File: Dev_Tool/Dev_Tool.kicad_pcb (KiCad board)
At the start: 4 copper layers, 159.8 x 100 mm, 146 parts, among them J1 UE27-BC54-100, J10 Conn_02x02_Odd_Even, J11 Conn_01x01_Pin, J12 Conn_01x01_Pin, J13 Conn_01x01_Pin, J14 Conn_01x01_Pin, J2 GSB12121031EU, J3 Conn_01x04, J4 95501-2881, J5 95501-2881, J6 JTAG, J7 Conn_02x08_Odd_Even, J8 Conn_02x08_Odd_Even, J9 Conn_02x04_Odd_Even, Q1 BSS138, Q2 BSS138, SW1 SW_Push, U1 USB2514B-AEZC, U10 EPM7032SLC44-10, U11 SN74HCT245DWR, U12 SN74LVC1G07DBV, U13 SN74LVC1G07DBV, U14 SN74LVC1G07DBV, U15 SN74LVC1G07DBV, U16 SN74LVC1G07DBV, U17 SN74LVC1G07DBV, U18 SN74LVC1G07DBV, U19 SN74LVC1G07DBV, U2 MIC2026-1YM, U20 SN74LVC1G07DBV, U21 SN74LVC1G07DBV, U22 SN74LVC1G07DBV, U23 LM1117-3.3, U24 APX803-31SAG-7, U25 SN74LVC1G07DBV, U26 USBLC6-2SC6, U27 USBLC6-2SC6, U3 24C02C-I/P, U4 MCP2221A-I/ST, U5 PCA9535PW, U6 FT232RNL, U7 MAX3243ECDB, U8 FT232RNL, U9 MAX3243ECDB, X1 DIN41612_03x32_ABC_COMETbus, Y1 ECS-3963-240-BN

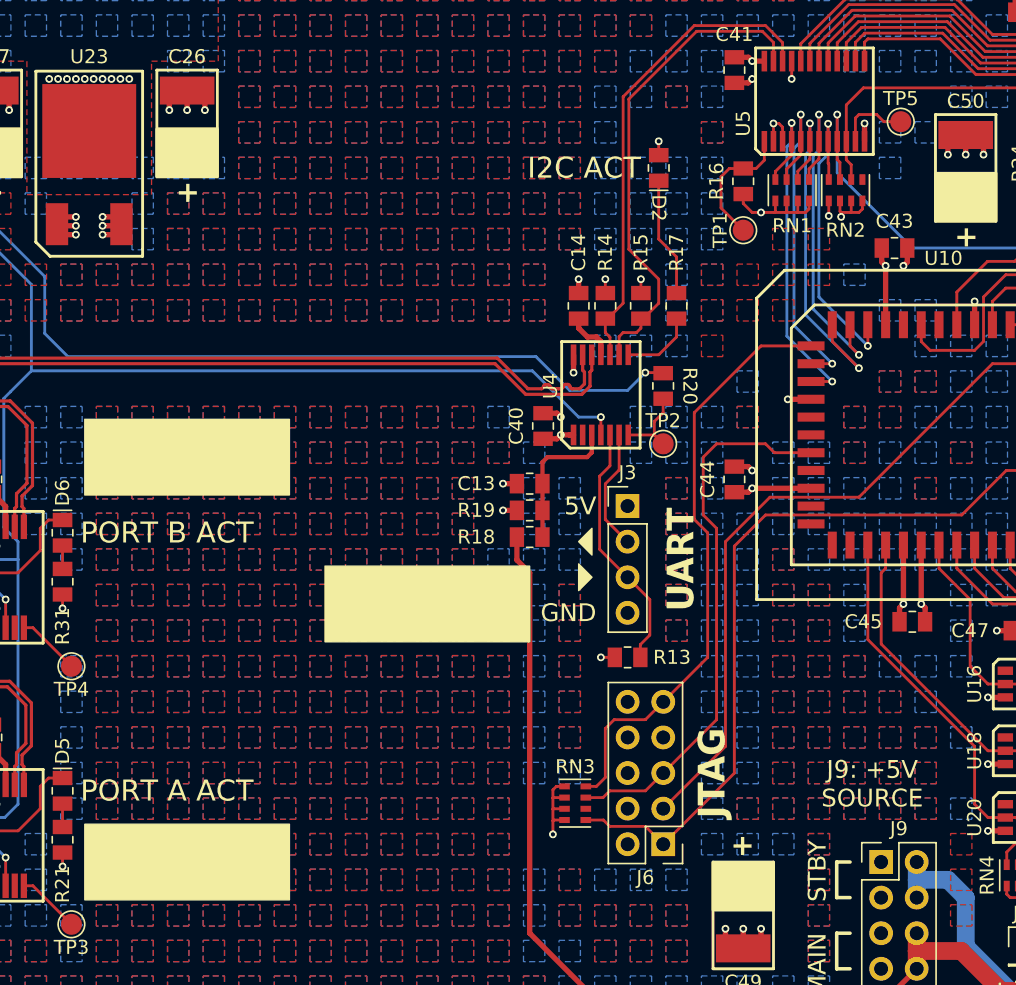
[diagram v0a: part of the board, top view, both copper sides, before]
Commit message: Further changes for rev 2
* Since the IN USE LED was moved to the MCP2221A, this freed up a GPIO on the PCA9535. Connect this to the SYSRESET signal so that it can be monitored during reset operations
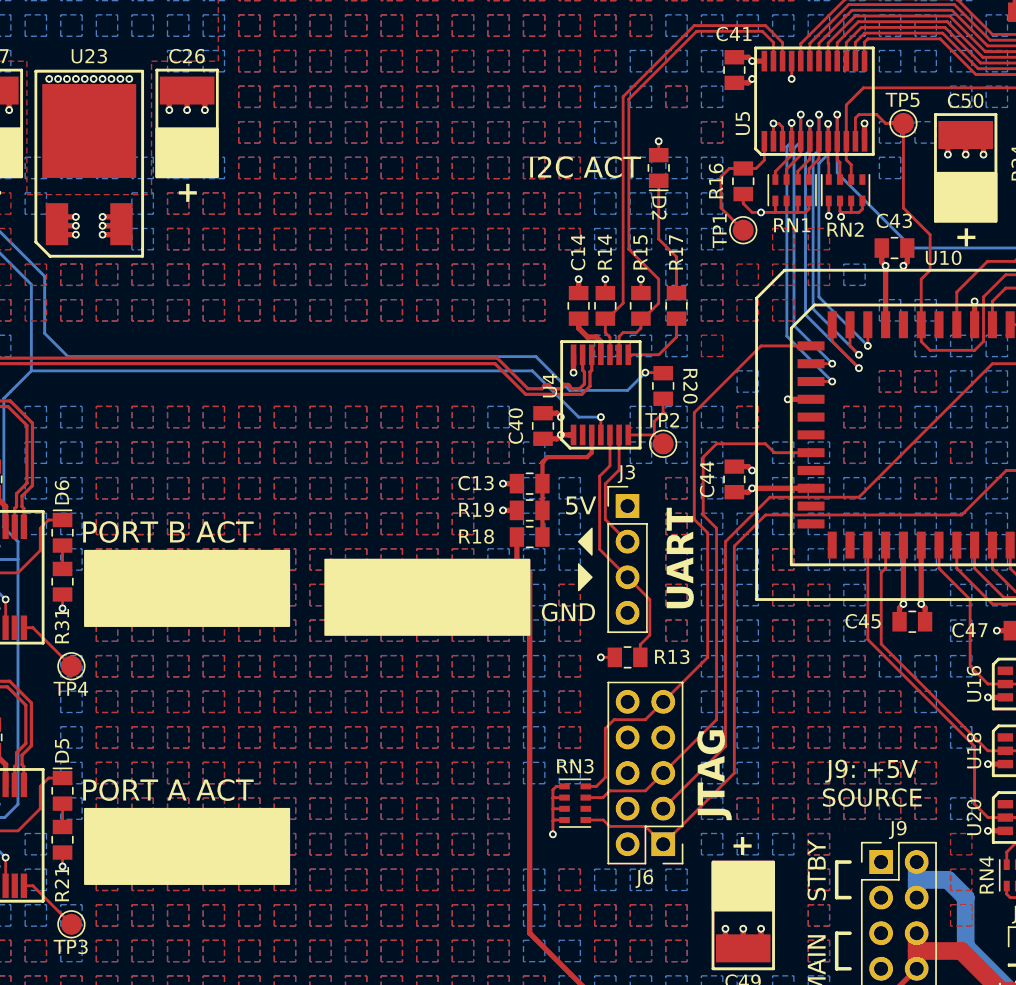
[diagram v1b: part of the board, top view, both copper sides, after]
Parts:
- moved TP5 0.23 mm to (190.2, 81.9)
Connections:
- TP5 pad 1: Net-(U5A-IO0_7) -> ~{SYSRESET}
- U5 pad 11: Net-(U5A-IO0_7) -> ~{SYSRESET}
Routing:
- net ~{SYSRESET}: track 30.1 -> 51.0 mm
- net Net-(U5A-IO0_7): track 5.21 -> 0.00 mm

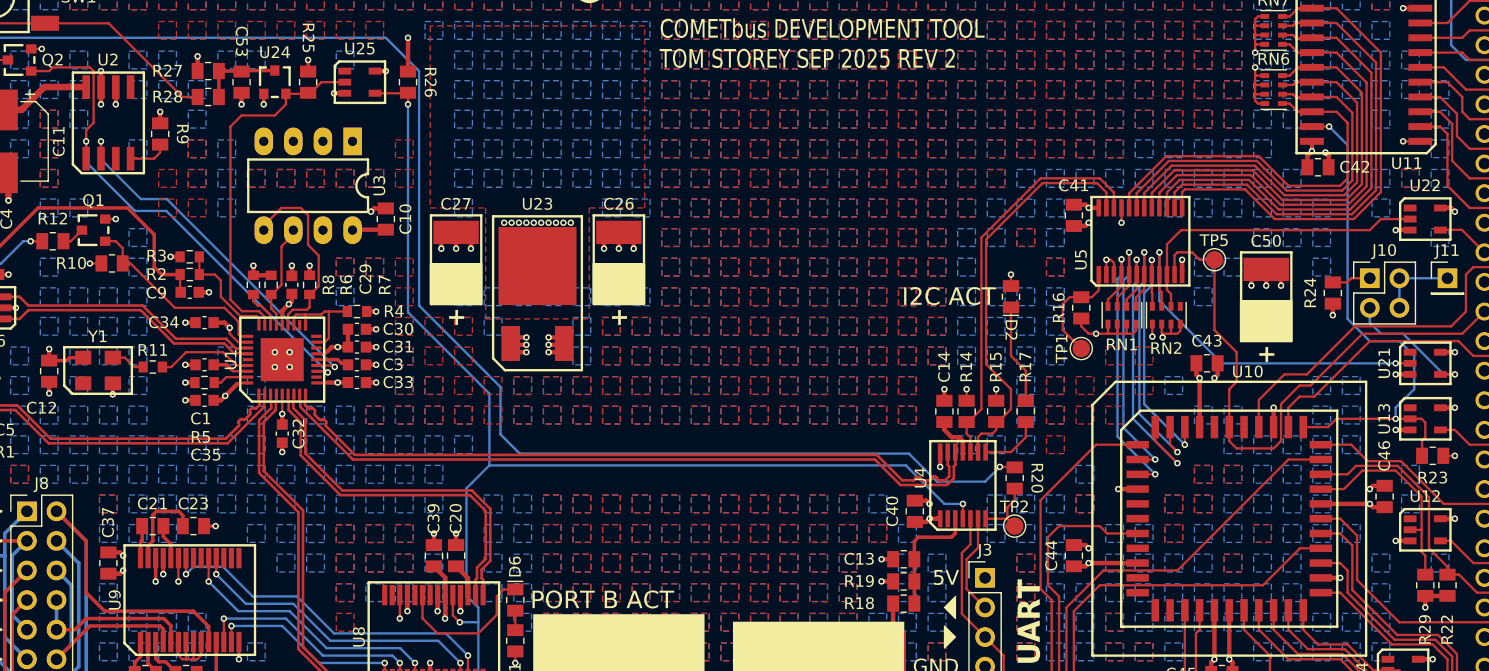
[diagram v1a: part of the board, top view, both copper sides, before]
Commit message: Add reset for 5V devices when hub is suspended
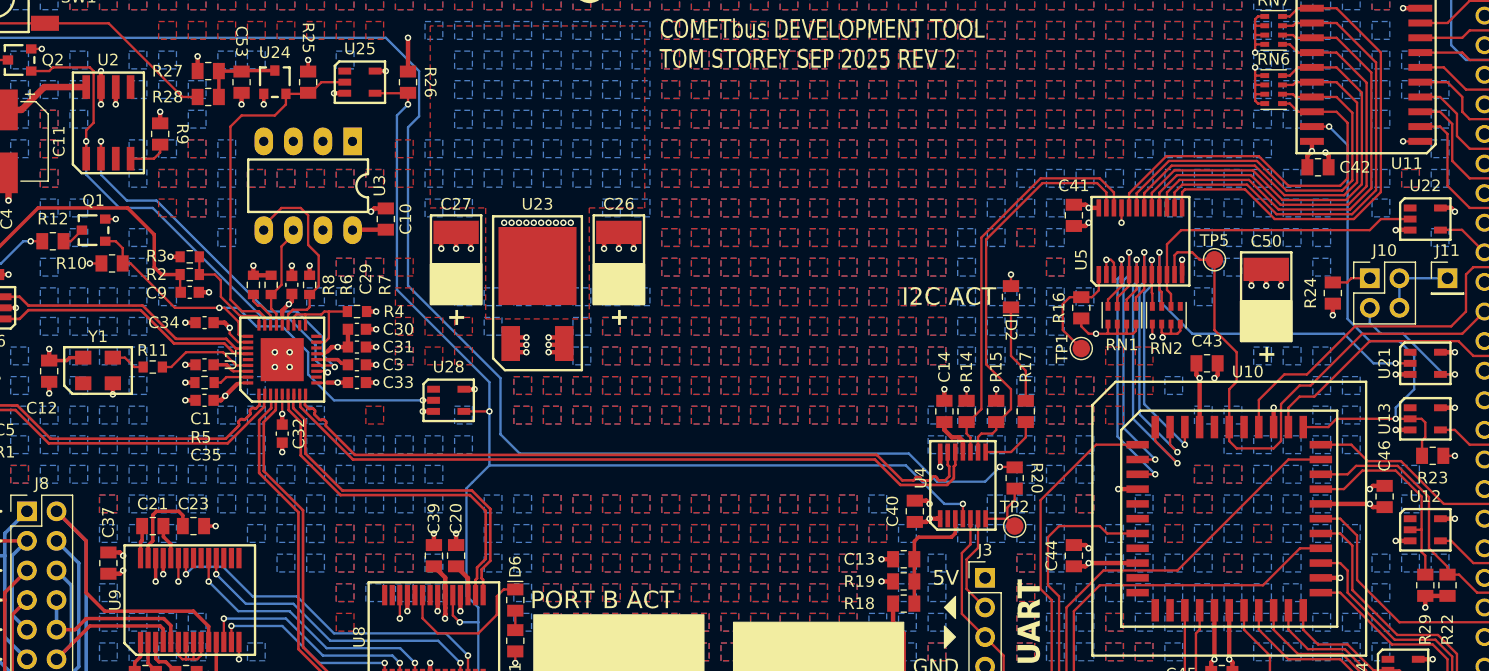
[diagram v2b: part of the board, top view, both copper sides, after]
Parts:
- added U28: SN74LVC1G07DBV, COMET_footprints:Package_SOT23-5, F.Cu at (124.5, 94.0)
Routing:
- net /USB hub/SUSP_IND: track 17.0 -> 39.8 mm, vias 0 -> 2
- net ~{RESET5}: track 121.9 -> 124.9 mm, vias 4 -> 5
- net ~{OCS1}: track 32.1 -> 33.8 mm
- net PRTPWR1: track 44.4 -> 45.8 mm
- net +5V: track 158.3 -> 159.3 mm, vias 65 -> 66
- net GND: track 158.4 -> 159.4 mm, vias 108 -> 109
- net Net-(D3-K): track 136.7 -> 137.5 mm

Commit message: Fix part number of I2C EEPROM
* The specified part number was not capable of running at 3.3V (manufacturer specified 4.5-5V, although it seems to work correctly on the board that I have built)
* The new part number has a manufacturer specified operating voltage range from 2.5-5V
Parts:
- U3: value 24C02C-I/P -> 24LC02B-I/P
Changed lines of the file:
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@@
 			)
 		)
-		(property "Value" "24C02C-I/P"
+		(property "Value" "24LC02B-I/P"
 			(at 0 6.14 90)
 			(layer "F.Fab")
